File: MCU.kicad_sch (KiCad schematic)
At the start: 96 parts, among them J501 HX JN1.27-2x5P ZZ H4.9, J502 Header, U501 STM32G431K8Tx, Y501 20 MHz

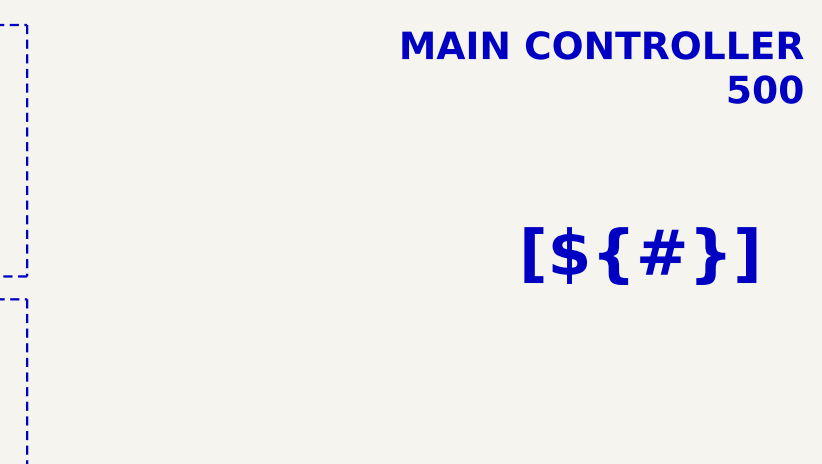
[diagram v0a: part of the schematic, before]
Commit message: Reworked sheet titles
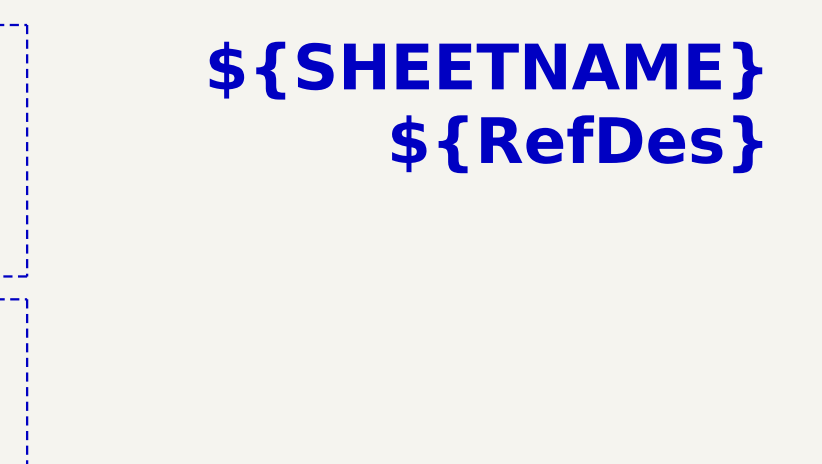
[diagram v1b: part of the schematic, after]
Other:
- note removed: "MAIN CONTROLLER 500"
- title: (none) -> ${SHEETNAME}
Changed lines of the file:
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@@
 	(paper "A4")
 	(title_block
+		(title "${SHEETNAME}")
 		(date "2025-01-12")
 	)
@@
 		(fill
 			(type none)
-		)
-	)
-	(text "MAIN CONTROLLER\n500"
-		(exclude_from_sim no)
-		(at 283.21 19.05 0)
-		(effects
-			(font
-				(size 3.048 3.048)
-				(thickness 0.4064)
-				(bold yes)
-				(color 0 0 255 1)
-			)
-			(justify right)
 		)
 	)
@@
 		)
 	)
-	(text_box "[${#}] ${TITLE}"
+	(text_box "${SHEETNAME}\n${RefDes}"
 		(exclude_from_sim no)
-		(at 182.88 33.02 0)
-		(size 101.6 12.7)
-		(margins 5.9999 5.9999 5.9999 5.9999)
+		(at 228.6 15.24 0)
+		(size 53.34 15.24)
+		(margins 2.54 1.27 2.54 1.27)
 		(stroke
 			(width -0.0001)

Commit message: Added PCB
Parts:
- removed P544: ~, symbol personal:Cosmetic_GND
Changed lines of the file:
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@@
 	(title_block
 		(title "${SHEETNAME}")
-		(date "2025-01-12")
+		(date "2025-07-04")
 	)
 	(rectangle
@@
 		(at 228.6 15.24 0)
 		(size 53.34 15.24)
-		(margins 2.54 1.27 2.54 1.27)
+		(margins 1.27 1.27 1.27 1.27)
 		(stroke
 			(width -0.0001)
@@
 	(wire
 		(pts
-			(xy 76.2 95.25) (xy 76.2 99.06)
-		)
-		(stroke
-			(width 0)
-			(type default)
-		)
-	)
-	(wire
-		(pts
 			(xy 204.47 107.95) (xy 204.47 104.14)
 		)
@@
 	(wire
 		(pts
-			(xy 72.39 95.25) (xy 76.2 95.25)
-		)
-		(stroke
-			(width 0)
-			(type default)
-		)
-	)
-	(wire
-		(pts
 			(xy 156.21 104.14) (xy 156.21 105.41)
 		)
@@
 		)
 	)
-	(wire
-		(pts
-			(xy 72.39 95.25) (xy 72.39 96.52)
-		)
-		(stroke
-			(width 0)
-			(type default)
-		)
-	)
 	(label "SH0"
 		(at 152.4 73.66 0)
@@
 	)
 	(label "SH0"
-		(at 72.39 96.52 180)
-		(effects
-			(font
-				(size 0.762 0.762)
-			)
-			(justify right bottom)
-		)
-	)
-	(label "SH0"
 		(at 76.2 114.3 0)
 		(effects
@@
 	)
 	(symbol
-		(lib_name "Cosmetic_PWR_4")
 		(lib_id "personal:Cosmetic_PWR")
 		(at 82.55 60.96 0)
@@
 			)
 		)
-		(property "Description" ""
+		(property "Description" "Local power symbol (sink), cosmetic use only"
 			(at 82.55 60.96 0)
 			(effects
@@
 		(dnp no)
 		(property "Reference" "C505"
-			(at 68.58 106.6799 0)
+			(at 67.31 106.68 0)
 			(effects
 				(font
@@
 		)
 		(property "Value" "22p"
-			(at 68.58 109.2199 0)
+			(at 67.31 109.22 0)
 			(effects
 				(font
@@
 	)
 	(symbol
-		(lib_name "Cosmetic_PWR_4")
 		(lib_id "personal:Cosmetic_PWR")
 		(at 123.19 72.39 0)
@@
 			)
 		)
-		(property "Description" ""
+		(property "Description" "Local power symbol (sink), cosmetic use only"
 			(at 123.19 72.39 0)
 			(effects
@@
 	)
 	(symbol
-		(lib_name "Cosmetic_PWR_4")
 		(lib_id "personal:Cosmetic_PWR")
 		(at 204.47 104.14 0)
@@
 			)
 		)
-		(property "Description" ""
+		(property "Description" "Local power symbol (sink), cosmetic use only"
 			(at 204.47 104.14 0)
 			(effects
@@
 	)
 	(symbol
-		(lib_name "Cosmetic_PWR_4")
 		(lib_id "personal:Cosmetic_PWR")
 		(at 181.61 27.94 0)
@@
 			)
 		)
-		(property "Description" ""
+		(property "Description" "Local power symbol (sink), cosmetic use only"
 			(at 181.61 27.94 0)
 			(effects
@@
 		(on_board yes)
 		(dnp no)
-		(fields_autoplaced yes)
 		(property "Reference" "C503"
-			(at 114.3 66.0399 0)
+			(at 113.03 66.04 0)
 			(effects
 				(font
@@
 		)
 		(property "Value" "100n"
-			(at 114.3 68.5799 0)
+			(at 113.03 68.58 0)
 			(effects
 				(font
@@
 		(on_board yes)
 		(dnp no)
-		(fields_autoplaced yes)
 		(property "Reference" "R506"
-			(at 138.43 55.88 90)
+			(at 138.43 57.15 90)
 			(effects
 				(font
@@
 		)
 		(property "Value" "0R"
-			(at 138.43 58.42 90)
+			(at 138.43 59.69 90)
 			(effects
 				(font
@@
 	)
 	(symbol
-		(lib_id "personal:Cosmetic_GND")
-		(at 72.39 96.52 0)
-		(unit 1)
-		(exclude_from_sim no)
-		(in_bom no)
-		(on_board no)
-		(dnp no)
-		(fields_autoplaced yes)
-		(property "Reference" "P544"
-			(at 72.39 95.504 0)
-			(effects
-				(font
-					(size 1.27 1.27)
-				)
-				(hide yes)
-			)
-		)
-		(property "Value" "~"
-			(at 74.93 97.7138 0)
-			(effects
-				(font
-					(size 1.27 1.27)
-				)
-				(justify left)
-				(hide yes)
-			)
-		)
-		(property "Footprint" ""
-			(at 72.39 96.52 0)
-			(effects
-				(font
-					(size 1.27 1.27)
-				)
-				(hide yes)
-			)
-		)
-		(property "Datasheet" ""
-			(at 72.39 96.52 0)
-			(effects
-				(font
-					(size 1.27 1.27)
-				)
-				(hide yes)
-			)
-		)
-		(property "Description" ""
-			(at 72.39 96.52 0)
-			(effects
-				(font
-					(size 1.27 1.27)
-				)
-				(hide yes)
-			)
-		)
-		(pin "1"
-		)
-		(instances
-			(project "Strobe_main"
-				(path "/f9e05184-c88b-4a88-ae9c-ab2bdb32be7c/82da9dbf-ba38-4d08-ba35-a220fa2963b1/ff259134-84db-47d3-8250-13ef5aa350b1"
-					(reference "P544")
-					(unit 1)
-				)
-			)
-		)
-	)
-	(symbol
 		(lib_id "Connector:Conn_01x02_Pin")
 		(at 210.82 107.95 0)
@@
 	)
 	(symbol
-		(lib_name "Cosmetic_PWR_4")
 		(lib_id "personal:Cosmetic_PWR")
 		(at 248.92 97.79 0)
@@
 			)
 		)
-		(property "Description" ""
+		(property "Description" "Local power symbol (sink), cosmetic use only"
 			(at 248.92 97.79 0)
 			(effects
@@
 			)
 		)
-		(property "Description" ""
+		(property "Description" "Local power symbol (source), cosmetic use only"
 			(at 35.56 24.13 0)
 			(effects
@@
 		(on_board yes)
 		(dnp no)
-		(fields_autoplaced yes)
 		(property "Reference" "C501"
-			(at 88.9 66.0399 0)
+			(at 87.63 66.04 0)
 			(effects
 				(font
@@
 		)
 		(property "Value" "1u"
-			(at 88.9 68.5799 0)
+			(at 87.63 68.58 0)
 			(effects
 				(font
@@
 	)
 	(symbol
-		(lib_name "Cosmetic_PWR_4")
 		(lib_id "personal:Cosmetic_PWR")
 		(at 143.51 27.94 0)
@@
 			)
 		)
-		(property "Description" ""
+		(property "Description" "Local power symbol (sink), cosmetic use only"
 			(at 143.51 27.94 0)
 			(effects
@@
 		(on_board yes)
 		(dnp no)
-		(fields_autoplaced yes)
 		(property "Reference" "R507"
-			(at 125.73 76.1999 0)
+			(at 124.46 76.2 0)
 			(effects
 				(font
@@
 		)
 		(property "Value" "10k"
-			(at 125.73 78.7399 0)
+			(at 124.46 78.74 0)
 			(effects
 				(font
@@
 		(on_board yes)
 		(dnp no)
-		(fields_autoplaced yes)
 		(property "Reference" "C502"
-			(at 101.6 66.0399 0)
+			(at 100.33 66.04 0)
 			(effects
 				(font
@@
 		)
 		(property "Value" "100n"
-			(at 101.6 68.5799 0)
+			(at 100.33 68.58 0)
 			(effects
 				(font
@@
 		(on_board yes)
 		(dnp no)
-		(fields_autoplaced yes)
 		(property "Reference" "C504"
-			(at 156.21 66.0399 0)
+			(at 154.94 66.04 0)
 			(effects
 				(font
@@
 		)
 		(property "Value" "100n"
-			(at 156.21 68.5799 0)
+			(at 154.94 68.58 0)
 			(effects
 				(font
